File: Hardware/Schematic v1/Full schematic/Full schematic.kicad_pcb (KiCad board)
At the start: 2 copper layers, 120 x 48.3 mm, 303 parts, among them J1 Conn_01x02_Male, J10 Conn_01x03_Male, J2 Reset, J3 Encoder, J4 Failure LED, J5 Bluetooth, J6 Conn_01x02_Male, J7 Display, J8 Buttons, J9 Conn_01x02_Male, K1 IM43TS, K2 IM43TS, K3 IM43TS, K4 IM43TS, K5 IM43TS, K6 IM43TS, Q1 BC847, Q10 IRLML6402, Q11 BC847, Q12 IRFZ44, Q13 BC847, Q14 IRLML6402, Q15 BC847, Q16 BSS138, Q17 BC847, Q18 IRF610, Q19 BC847, Q2 BC847, Q20 IRLML6402, Q21 BC847, Q22 IRLML6402, Q23 BFS17, Q24 AFT05MS003N, Q3 BC847, Q4 BC847, Q5 BC847, Q6 IRLML6402, Q7 IRF4905, Q8 IRLML6402, Q9 IRLML6402, U1 74LVC2T45DC, U10 ICS501, U11 STM32F103C8Tx, U12 MCP23017_SS, U13 CAT24C256, U2 74LVC2T45DC, U3 AD9835, U4 LM27313XMF, U5 LM2734X, U6 LM2734X, U7 MAX1837EUT33-T, U8 UC3843_SOIC8, U9 AD5245BRJZ10, X1 50MHz, Y1 8MHz, Y2 32768Hz

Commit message: PCB tracing is close to an end
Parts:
- removed JP1: BOOT0, Connector_PinHeader_2.54mm:PinHeader_1x03_P2.54mm_Vertical
- removed JP2: BOOT1, Connector_PinHeader_2.54mm:PinHeader_1x03_P2.54mm_Vertical
- C11, C32, C44, C6, C74, C76, C79, C83, C84, C87, C91, C94, C95, C97, D1, D2, D3, J10, J2, J3, J4, J5, J7, J8, L5, R10, R12, R14, R15, R16, R18, R20, R21, R22, R24, R40, R49, R6, R72, R8, R80, R83, R86, R9, R92, R93, R94, R95, Y1: moved to B.Cu
- Y2: footprint Crystal:Crystal_C26-LF_D2.1mm_L6.5mm_Horizontal_1EP_style1 -> Crystal:Crystal_C26-LF_D2.1mm_L6.5mm_Vertical; moved to B.Cu
- moved D12 243.6 mm to (315.7, 51.9)
- moved U13 232.2 mm to (286.7, 63.8)
- moved D13 230.3 mm to (313.2, 47.2), turned to 180 degrees
- moved R73 209.2 mm to (319.2, 51.3), turned to 90 degrees
- moved R77 208.8 mm to (315.2, 49.0), turned to -90 degrees
- moved Y1 207.8 mm to (278.0, 85.3), turned to 180 degrees
- moved J5 204.0 mm to (265.3, 71.4), turned to 180 degrees
- moved J3 198.8 mm to (278.5, 69.8), turned to -90 degrees
- moved U11 191.9 mm to (276.1, 76.6), turned to 90 degrees
- moved J8 190.2 mm to (286.4, 81.9), turned to 180 degrees
- moved C32 188.7 mm to (273.1, 63.3), turned to 90 degrees
- moved C88 180.0 mm to (290.2, 86.0), turned to -90 degrees
- moved R86 178.4 mm to (280.8, 72.6), turned to 180 degrees
- moved C74 177.2 mm to (283.6, 66.8), turned to 90 degrees
- moved C30 176.4 mm to (254.9, 62.5), turned to -90 degrees
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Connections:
- U11 pad 14: BTN_LEFT -> BTN_RIGHT
- U11 pad 16: BTN_RIGHT -> BTN_LEFT
- U11 pad 20: BOOT1 -> unconnected-(U11-Pad20)
- U11 pad 25: ENCODER_L -> ENCODER_BTN
- U11 pad 27: ENCODER_BTN -> ENCODER_L
- U11 pad 44: BOOT0 -> GND
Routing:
- net GND: track 479.7 -> 743.0 mm, vias 35 -> 46
- net PWR_144_OUT: track 13.7 -> 120.8 mm, vias 0 -> 1
- net PWR_3.5_12: track 19.6 -> 117.6 mm, vias 5 -> 6
- net PWR_144_5: track 56.9 -> 151.2 mm
- net SW_3.3V: track 18.7 -> 103.4 mm, vias 3 -> 9
- net PWR_3.5_5: track 6.44 -> 87.7 mm, vias 1 -> 2
- net I2C2_SCL: track 1.93 -> 68.8 mm, vias 1 -> 3
- net I2C2_SDA: track 1.96 -> 66.8 mm, vias 1 -> 4
- net COMM_5V_ENABLE: track 0.00 -> 49.5 mm, vias 0 -> 4
- net PWR_3.5_OUT: track 14.7 -> 62.8 mm, vias 0 -> 1
- net REG_3.3V: track 0.00 -> 47.5 mm, vias 0 -> 8
- net ACTIVATE_DISPLAY: track 0.00 -> 44.3 mm, vias 0 -> 4
- net ACTIVATE_3.5: track 0.00 -> 43.7 mm, vias 0 -> 4
- net ACTIVATE_144: track 0.00 -> 40.1 mm, vias 0 -> 1
- net DISPLAY_4V: track 11.9 -> 48.7 mm, vias 2 -> 5
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
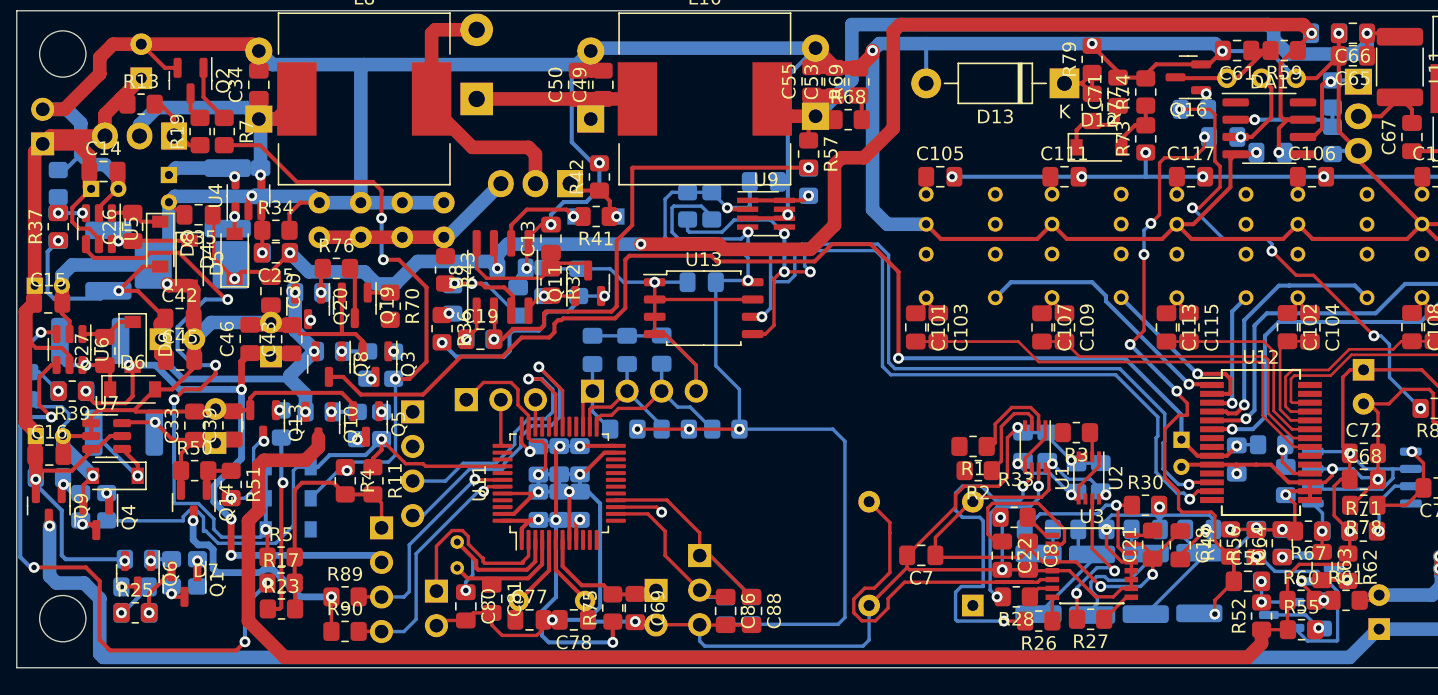
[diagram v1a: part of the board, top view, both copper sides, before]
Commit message: Traced all connections, now need to fill everything with ground
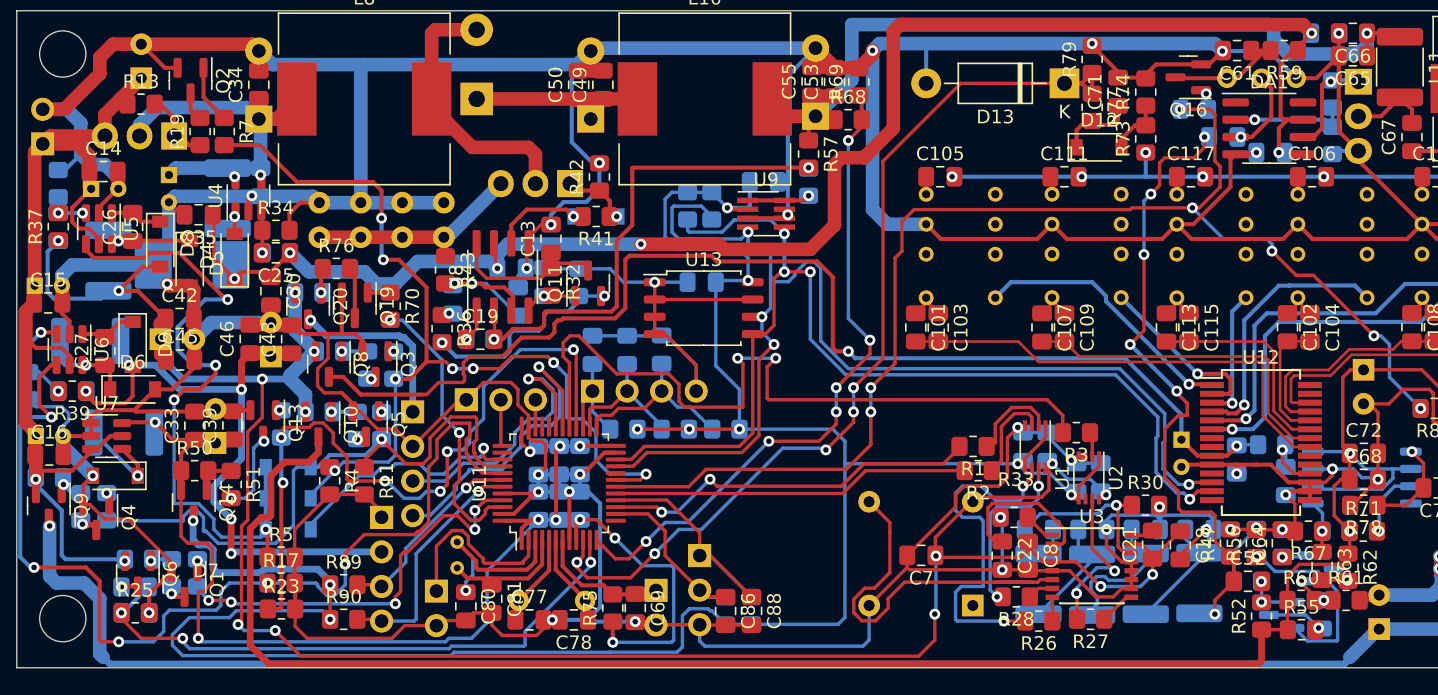
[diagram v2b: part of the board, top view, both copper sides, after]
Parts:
- moved R4 1.14 mm to (259.2, 76.4)
- moved R89 0.89 mm to (260.2, 84.1)
- moved R90 0.89 mm to (260.2, 86.6)
- moved J7 0.77 mm to (263.0, 79.1)
- moved R11 0.63 mm to (261.7, 76.4)
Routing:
- net REG_5V: track 88.8 -> 166.5 mm, vias 9 -> 14
- net SW_3.3V: track 103.4 -> 173.4 mm, vias 9 -> 10
- net ADC_UANT: track 4.95 -> 68.4 mm, vias 0 -> 5
- net Manipulation: track 35.6 -> 94.7 mm, vias 5 -> 7
- net DDS_FSYNC: track 0.00 -> 55.9 mm, vias 0 -> 2
- net REG_3.3V: track 47.5 -> 95.7 mm, vias 8 -> 10
- net ADC_U3.5_OUT: track 1.87 -> 48.7 mm, vias 0 -> 6
- net ADC_UBATT: track 2.79 -> 43.8 mm, vias 1 -> 3
- net ACTIVATE_3.3V: track 13.6 -> 53.0 mm, vias 1 -> 6
- net ACTIVATE_DISPLAY: track 44.3 -> 74.3 mm, vias 4 -> 5
- net ENABLE_UBATT_CHECK: track 0.00 -> 29.9 mm, vias 0 -> 5
- net GND: track 743.0 -> 769.9 mm
- net DDS_SDATA: track 0.00 -> 26.3 mm
- net ACTIVATE_3.5: track 43.7 -> 69.2 mm, vias 4 -> 8
- net DDS_SCLK: track 3.52 -> 27.9 mm, vias 1 -> 2
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
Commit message: PCB seems to be production-ready
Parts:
- D13: moved to B.Cu
- moved R54 219.1 mm to (104.8, 26.7), turned to 90 degrees
- moved R90 218.8 mm to (42.7, 63.1)
- moved J7 218.8 mm to (45.5, 55.6)
- moved R89 218.8 mm to (42.7, 60.6)
- moved C92 218.6 mm to (132.7, 62.8)
- moved C112 218.1 mm to (123.7, 30.6)
- moved C3 218.1 mm to (97.3, 52.7)
- moved C64 218.1 mm to (112.4, 57.5)
- moved C68 218.1 mm to (118.4, 52.8)
- moved C71 218.1 mm to (100.3, 24.4)
- moved C72 218.1 mm to (118.4, 50.9)
- moved L8 218.1 mm to (45.0, 24.9)
- moved R47 218.1 mm to (108.6, 57.5)
- moved R52 218.1 mm to (110.9, 62.9)
- moved R57 218.1 mm to (77.6, 28.9)
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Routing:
- net GND: track 769.9 -> 785.2 mm, vias 46 -> 304
- net ANT_3.5: track 60.5 -> 71.2 mm
- net REG_3.3V: track 95.7 -> 101.7 mm
- net Net-(Q16-Pad1): track 1.20 -> 4.02 mm
- net DDS_FSYNC: track 55.9 -> 53.3 mm
- net SW_3.3V: track 173.4 -> 171.9 mm
- net DISPLAY_4V: track 48.7 -> 47.6 mm
- net DISPLAY_SCL: track 14.6 -> 15.4 mm
- net DISPLAY_SDA: track 17.6 -> 18.4 mm
- net Manipulation: vias 7 -> 5
- net ADC_UANT: vias 5 -> 3
- net ADC_U3.5_OUT: vias 6 -> 4
- added copper zone on B.Cu, net GND
- added copper zone on F.Cu, net GND
